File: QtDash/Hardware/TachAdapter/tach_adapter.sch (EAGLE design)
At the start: 10 parts, among them IC1 TLP293

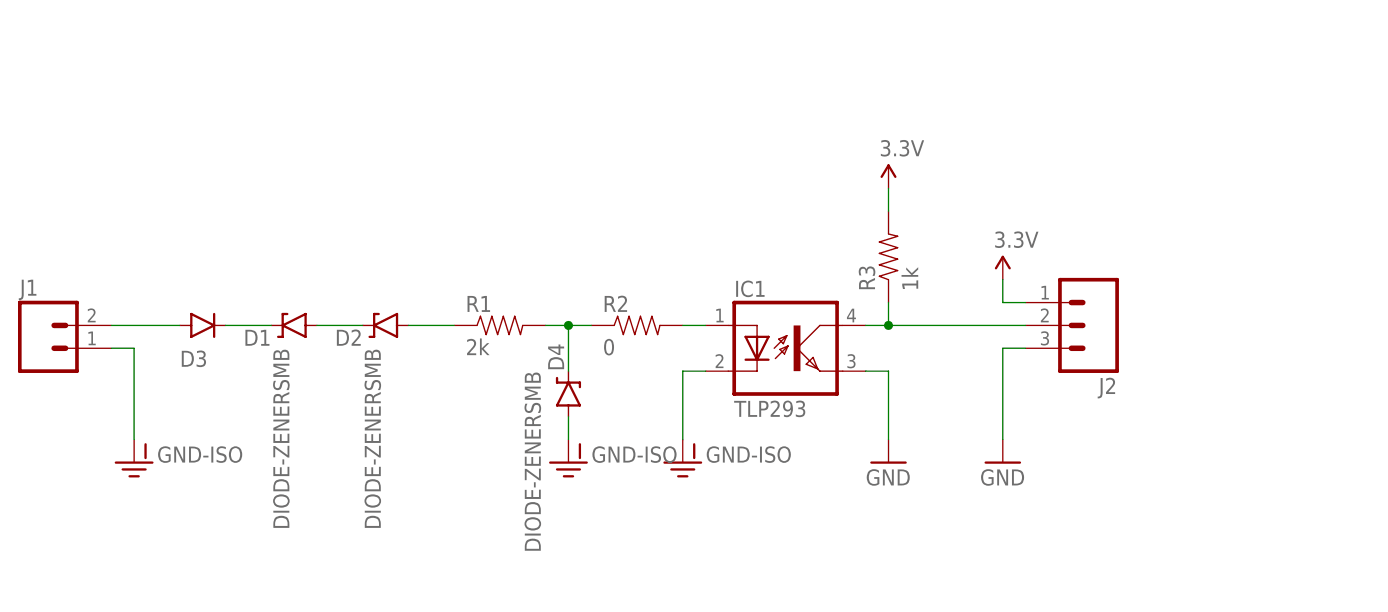
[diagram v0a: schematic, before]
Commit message: - updated tach adapter with opto-coupler that is currently available 	- added datasheets for tach-adapter components 	- updated dashhat library with new connector 31 dimensions 	- moved circuit simulations into their own folder
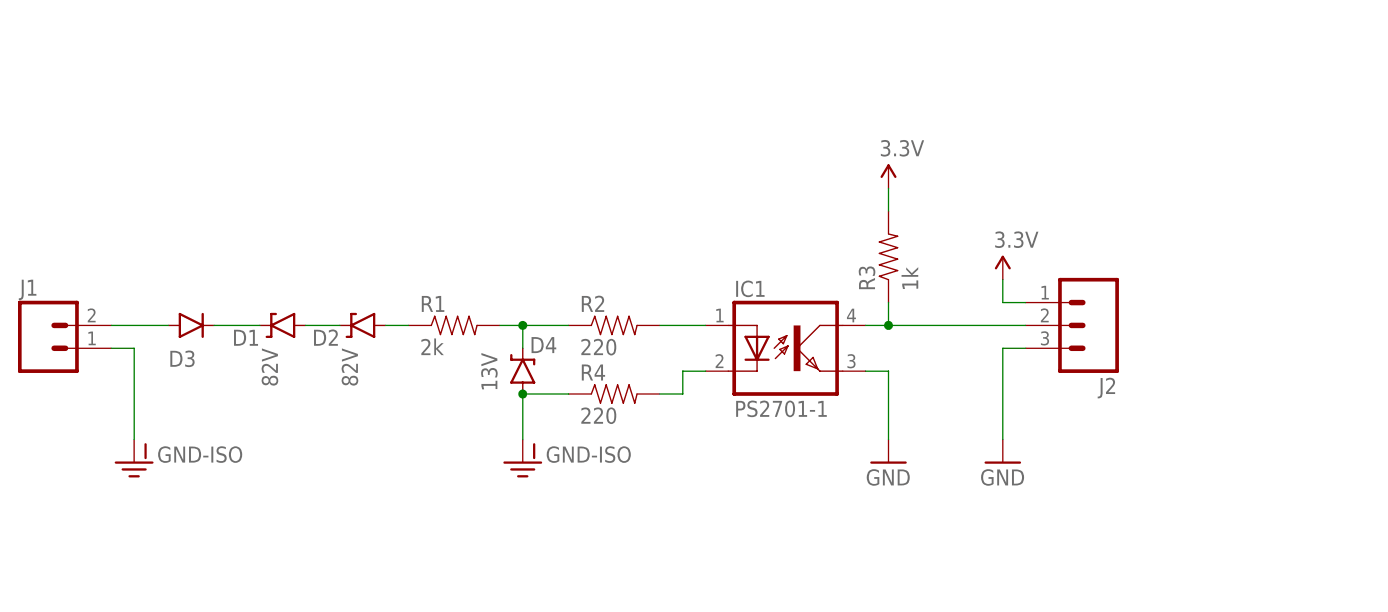
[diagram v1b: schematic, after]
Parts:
- added R4: 220, SparkFun-Passives:RESISTOR1206
- D1, D2: value DIODE-ZENERSMB -> 82V
- D4: value DIODE-ZENERSMB -> 13V
- IC1: value TLP293 -> PS2701-1; device tach_adapter:TLP293 -> tach_adapter:PS2701-1
- R2: value 0 -> 220
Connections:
- new net N$6: IC1.C, R4.2
- net GND-ISO: now also R4.1; no longer IC1.C
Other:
- moved on the sheet: D1, D2, D3, D4, R1, R2
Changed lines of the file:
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@@
 <?xml version="1.0" encoding="utf-8"?>
 <!DOCTYPE eagle SYSTEM "eagle.dtd">
-<eagle version="7.1.0">
+<eagle version="7.7.0">
 <drawing>
 <settings>
@@
 <setting verticaltext="up"/>
 </settings>
-<grid distance="0.1" unitdist="inch" unit="inch" style="lines" multiple="1" display="no" altdistance="0.01" altunitdist="inch" altunit="inch"/>
+<grid distance="0.05" unitdist="inch" unit="inch" style="lines" multiple="1" display="no" altdistance="0.01" altunitdist="inch" altunit="inch"/>
 <layers>
 <layer number="1" name="Top" color="4" fill="1" visible="no" active="no"/>
@@
 </classes>
 <parts>
-<part name="D1" library="SparkFun-DiscreteSemi" deviceset="DIODE-ZENER" device="SMB"/>
-<part name="D2" library="SparkFun-DiscreteSemi" deviceset="DIODE-ZENER" device="SMB"/>
+<part name="D1" library="SparkFun-DiscreteSemi" deviceset="DIODE-ZENER" device="SMB" value="82V"/>
+<part name="D2" library="SparkFun-DiscreteSemi" deviceset="DIODE-ZENER" device="SMB" value="82V"/>
 <part name="D3" library="SparkFun-DiscreteSemi" deviceset="DIODE" device="SMA"/>
 <part name="R1" library="SparkFun-Passives" deviceset="RESISTOR" device="1206" value="2k"/>
-<part name="R2" library="SparkFun-Passives" deviceset="RESISTOR" device="1206" value="0"/>
-<part name="IC1" library="tach_adapter" deviceset="TLP293" device=""/>
+<part name="R2" library="SparkFun-Passives" deviceset="RESISTOR" device="1206" value="220"/>
+<part name="IC1" library="tach_adapter" deviceset="PS2701-1" device=""/>
 <part name="R3" library="SparkFun-Passives" deviceset="RESISTOR" device="0603-RES" value="1k"/>
 <part name="SUPPLY1" library="SparkFun-Aesthetics" deviceset="3.3V" device=""/>
 <part name="GND1" library="SparkFun-Aesthetics" deviceset="GND" device=""/>
-<part name="GND-ISO1" library="SparkFun-Aesthetics" deviceset="GND-ISO" device=""/>
-<part name="D4" library="SparkFun-DiscreteSemi" deviceset="DIODE-ZENER" device="SMB"/>
+<part name="D4" library="SparkFun-DiscreteSemi" deviceset="DIODE-ZENER" device="SMB" value="13V"/>
 <part name="GND-ISO2" library="SparkFun-Aesthetics" deviceset="GND-ISO" device=""/>
 <part name="J1" library="SparkFun-Connectors" deviceset="M02" device="PTH3"/>
@@
 <part name="SUPPLY2" library="SparkFun-Aesthetics" deviceset="3.3V" device=""/>
 <part name="GND2" library="SparkFun-Aesthetics" deviceset="GND" device=""/>
+<part name="R4" library="SparkFun-Passives" deviceset="RESISTOR" device="1206" value="220"/>
 </parts>
 <sheets>
@@
 </plain>
 <instances>
-<instance part="D1" gate="G$1" x="45.72" y="60.96" smashed="yes" rot="R180">
-<attribute name="NAME" x="43.18" y="60.4774" size="1.778" layer="95" rot="R180"/>
-<attribute name="VALUE" x="43.4086" y="58.42" size="1.778" layer="96" rot="R270"/>
+<instance part="D1" gate="G$1" x="44.45" y="60.96" smashed="yes" rot="R180">
+<attribute name="NAME" x="41.91" y="60.4774" size="1.778" layer="95" rot="R180"/>
+<attribute name="VALUE" x="42.1386" y="58.42" size="1.778" layer="96" rot="R270"/>
 </instance>
-<instance part="D2" gate="G$1" x="55.88" y="60.96" smashed="yes" rot="R180">
-<attribute name="NAME" x="53.34" y="60.4774" size="1.778" layer="95" rot="R180"/>
-<attribute name="VALUE" x="53.5686" y="58.42" size="1.778" layer="96" rot="R270"/>
+<instance part="D2" gate="G$1" x="53.34" y="60.96" smashed="yes" rot="R180">
+<attribute name="NAME" x="50.8" y="60.4774" size="1.778" layer="95" rot="R180"/>
+<attribute name="VALUE" x="51.0286" y="58.42" size="1.778" layer="96" rot="R270"/>
 </instance>
-<instance part="D3" gate="G$1" x="35.56" y="60.96" smashed="yes">
-<attribute name="NAME" x="33.02" y="56.3626" size="1.778" layer="95"/>
-<attribute name="VALUE" x="38.1" y="58.6486" size="1.778" layer="96"/>
+<instance part="D3" gate="G$1" x="34.29" y="60.96" smashed="yes">
+<attribute name="NAME" x="31.75" y="56.3626" size="1.778" layer="95"/>
+<attribute name="VALUE" x="36.83" y="58.6486" size="1.778" layer="96"/>
 </instance>
-<instance part="R1" gate="G$1" x="68.58" y="60.96"/>
-<instance part="R2" gate="G$1" x="83.82" y="60.96"/>
+<instance part="R1" gate="G$1" x="63.5" y="60.96"/>
+<instance part="R2" gate="G$1" x="81.28" y="60.96"/>
 <instance part="IC1" gate="G$1" x="101.6" y="58.42"/>
 <instance part="R3" gate="G$1" x="111.76" y="68.58" rot="R90"/>
 <instance part="SUPPLY1" gate="G$1" x="111.76" y="76.2"/>
 <instance part="GND1" gate="1" x="111.76" y="45.72"/>
-<instance part="GND-ISO1" gate="G$1" x="88.9" y="45.72"/>
-<instance part="D4" gate="G$1" x="76.2" y="53.34" smashed="yes" rot="R90">
-<attribute name="NAME" x="75.7174" y="55.88" size="1.778" layer="95" rot="R90"/>
-<attribute name="VALUE" x="71.3486" y="55.88" size="1.778" layer="96" rot="R270"/>
+<instance part="D4" gate="G$1" x="71.12" y="55.88" smashed="yes" rot="R90">
+<attribute name="NAME" x="71.882" y="57.8866" size="1.778" layer="95"/>
+<attribute name="VALUE" x="66.5226" y="57.912" size="1.778" layer="96" rot="R270"/>
 </instance>
-<instance part="GND-ISO2" gate="G$1" x="76.2" y="45.72"/>
+<instance part="GND-ISO2" gate="G$1" x="71.12" y="45.72"/>
 <instance part="J1" gate="G$1" x="17.78" y="58.42"/>
 <instance part="J2" gate="J$1" x="134.62" y="60.96" rot="R180"/>
@@
 <instance part="SUPPLY2" gate="G$1" x="124.46" y="66.04"/>
 <instance part="GND2" gate="1" x="124.46" y="45.72"/>
+<instance part="R4" gate="G$1" x="81.28" y="53.34"/>
 </instances>
 <busses>
@@
 <pinref part="D1" gate="G$1" pin="C"/>
 <pinref part="D3" gate="G$1" pin="C"/>
-<wire x1="43.18" y1="60.96" x2="38.1" y2="60.96" width="0.1524" layer="91"/>
+<wire x1="41.91" y1="60.96" x2="36.83" y2="60.96" width="0.1524" layer="91"/>
 </segment>
 </net>
@@
 <pinref part="D1" gate="G$1" pin="A"/>
 <pinref part="D2" gate="G$1" pin="C"/>
-<wire x1="48.26" y1="60.96" x2="53.34" y2="60.96" width="0.1524" layer="91"/>
+<wire x1="46.99" y1="60.96" x2="50.8" y2="60.96" width="0.1524" layer="91"/>
 </segment>
 </net>
@@
 <pinref part="D2" gate="G$1" pin="A"/>
 <pinref part="R1" gate="G$1" pin="1"/>
-<wire x1="58.42" y1="60.96" x2="63.5" y2="60.96" width="0.1524" layer="91"/>
+<wire x1="55.88" y1="60.96" x2="58.42" y2="60.96" width="0.1524" layer="91"/>
 </segment>
 </net>
@@
 <pinref part="R1" gate="G$1" pin="2"/>
 <pinref part="R2" gate="G$1" pin="1"/>
-<wire x1="73.66" y1="60.96" x2="76.2" y2="60.96" width="0.1524" layer="91"/>
+<wire x1="68.58" y1="60.96" x2="71.12" y2="60.96" width="0.1524" layer="91"/>
 <pinref part="D4" gate="G$1" pin="C"/>
-<wire x1="76.2" y1="60.96" x2="78.74" y2="60.96" width="0.1524" layer="91"/>
-<wire x1="76.2" y1="55.88" x2="76.2" y2="60.96" width="0.1524" layer="91"/>
-<junction x="76.2" y="60.96"/>
+<wire x1="71.12" y1="60.96" x2="76.2" y2="60.96" width="0.1524" layer="91"/>
+<wire x1="71.12" y1="58.42" x2="71.12" y2="60.96" width="0.1524" layer="91"/>
+<junction x="71.12" y="60.96"/>
 </segment>
 </net>
@@
 <pinref part="R2" gate="G$1" pin="2"/>
 <pinref part="IC1" gate="G$1" pin="A"/>
-<wire x1="88.9" y1="60.96" x2="91.44" y2="60.96" width="0.1524" layer="91"/>
+<wire x1="86.36" y1="60.96" x2="91.44" y2="60.96" width="0.1524" layer="91"/>
 </segment>
 </net>
@@
 <net name="GND-ISO" class="0">
 <segment>
-<pinref part="IC1" gate="G$1" pin="C"/>
-<wire x1="91.44" y1="55.88" x2="88.9" y2="55.88" width="0.1524" layer="91"/>
-<pinref part="GND-ISO1" gate="G$1" pin="GND-ISO"/>
-<wire x1="88.9" y1="55.88" x2="88.9" y2="48.26" width="0.1524" layer="91"/>
-</segment>
-<segment>
 <pinref part="D4" gate="G$1" pin="A"/>
-<wire x1="76.2" y1="50.8" x2="76.2" y2="48.26" width="0.1524" layer="91"/>
 <pinref part="GND-ISO2" gate="G$1" pin="GND-ISO"/>
+<pinref part="R4" gate="G$1" pin="1"/>
+<wire x1="71.12" y1="53.34" x2="71.12" y2="48.26" width="0.1524" layer="91"/>
+<wire x1="76.2" y1="53.34" x2="71.12" y2="53.34" width="0.1524" layer="91"/>
+<junction x="71.12" y="53.34"/>
 </segment>
 <segment>
@@
 <pinref part="D3" gate="G$1" pin="A"/>
 <pinref part="J1" gate="G$1" pin="2"/>
-<wire x1="25.4" y1="60.96" x2="33.02" y2="60.96" width="0.1524" layer="91"/>
-</segment>
-</net>
+<wire x1="25.4" y1="60.96" x2="31.75" y2="60.96" width="0.1524" layer="91"/>
+</segment>
+</net>
+<net name="N$6" class="0">
+<segment>
+<pinref part="IC1" gate="G$1" pin="C"/>
+<wire x1="91.44" y1="55.88" x2="88.9" y2="55.88" width="0.1524" layer="91"/>
+<wire x1="88.9" y1="55.88" x2="88.9" y2="53.34" width="0.1524" layer="91"/>
+<pinref part="R4" gate="G$1" pin="2"/>
+<wire x1="88.9" y1="53.34" x2="86.36" y2="53.34" width="0.1524" layer="91"/>
+</segment>
+</net>

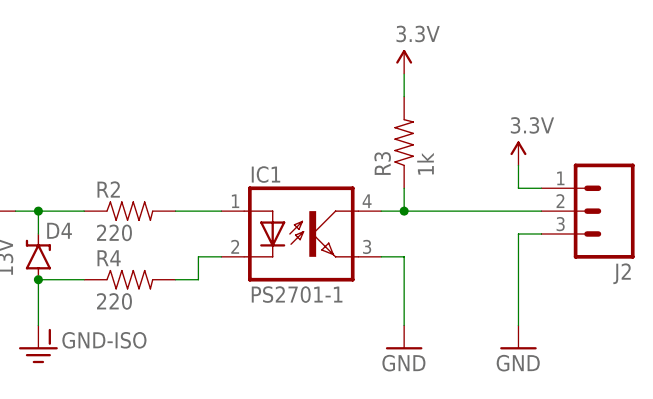
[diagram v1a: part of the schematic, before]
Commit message: - finished tach adapter board -- ordered components and board from OSHPark
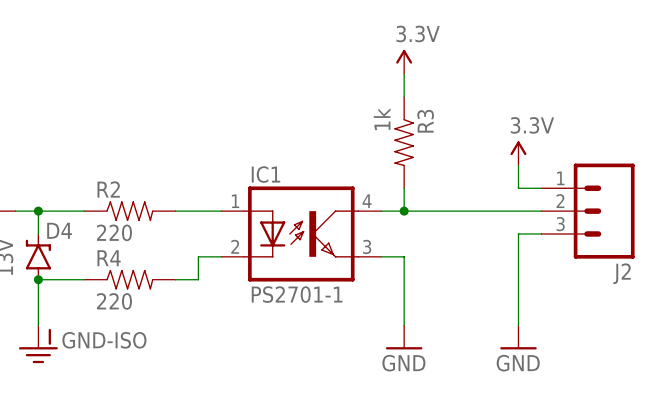
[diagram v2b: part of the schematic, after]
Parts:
- R3: device SparkFun-Passives:RESISTOR0603-RES -> SparkFun-Passives:RESISTOR1206
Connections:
- net 3.3V: now also R3.1; no longer R3.2
- net N$7: now also R3.2; no longer R3.1
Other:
- moved on the sheet: R3
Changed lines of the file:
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@@
 <setting verticaltext="up"/>
 </settings>
-<grid distance="0.05" unitdist="inch" unit="inch" style="lines" multiple="1" display="no" altdistance="0.01" altunitdist="inch" altunit="inch"/>
+<grid distance="0.1" unitdist="inch" unit="inch" style="lines" multiple="1" display="no" altdistance="0.01" altunitdist="inch" altunit="inch"/>
 <layers>
 <layer number="1" name="Top" color="4" fill="1" visible="no" active="no"/>
@@
 <part name="R2" library="SparkFun-Passives" deviceset="RESISTOR" device="1206" value="220"/>
 <part name="IC1" library="tach_adapter" deviceset="PS2701-1" device=""/>
-<part name="R3" library="SparkFun-Passives" deviceset="RESISTOR" device="0603-RES" value="1k"/>
 <part name="SUPPLY1" library="SparkFun-Aesthetics" deviceset="3.3V" device=""/>
 <part name="GND1" library="SparkFun-Aesthetics" deviceset="GND" device=""/>
@@
 <part name="GND2" library="SparkFun-Aesthetics" deviceset="GND" device=""/>
 <part name="R4" library="SparkFun-Passives" deviceset="RESISTOR" device="1206" value="220"/>
+<part name="R3" library="SparkFun-Passives" deviceset="RESISTOR" device="1206" value="1k"/>
 </parts>
 <sheets>
@@
 <instance part="R2" gate="G$1" x="81.28" y="60.96"/>
 <instance part="IC1" gate="G$1" x="101.6" y="58.42"/>
-<instance part="R3" gate="G$1" x="111.76" y="68.58" rot="R90"/>
 <instance part="SUPPLY1" gate="G$1" x="111.76" y="76.2"/>
 <instance part="GND1" gate="1" x="111.76" y="45.72"/>
@@
 <instance part="GND2" gate="1" x="124.46" y="45.72"/>
 <instance part="R4" gate="G$1" x="81.28" y="53.34"/>
+<instance part="R3" gate="G$1" x="111.76" y="68.58" rot="R270"/>
 </instances>
 <busses>
@@
 <wire x1="109.22" y1="60.96" x2="111.76" y2="60.96" width="0.1524" layer="91"/>
 <wire x1="111.76" y1="60.96" x2="111.76" y2="63.5" width="0.1524" layer="91"/>
-<pinref part="R3" gate="G$1" pin="1"/>
 <pinref part="J2" gate="J$1" pin="2"/>
 <wire x1="127" y1="60.96" x2="111.76" y2="60.96" width="0.1524" layer="91"/>
 <junction x="111.76" y="60.96"/>
+<pinref part="R3" gate="G$1" pin="2"/>
 </segment>
 </net>
 <net name="3.3V" class="0">
 <segment>
-<pinref part="R3" gate="G$1" pin="2"/>
 <pinref part="SUPPLY1" gate="G$1" pin="3.3V"/>
 <wire x1="111.76" y1="73.66" x2="111.76" y2="76.2" width="0.1524" layer="91"/>
-</segment>
-<segment>
+<pinref part="R3" gate="G$1" pin="1"/>
+</segment>
+<segment>

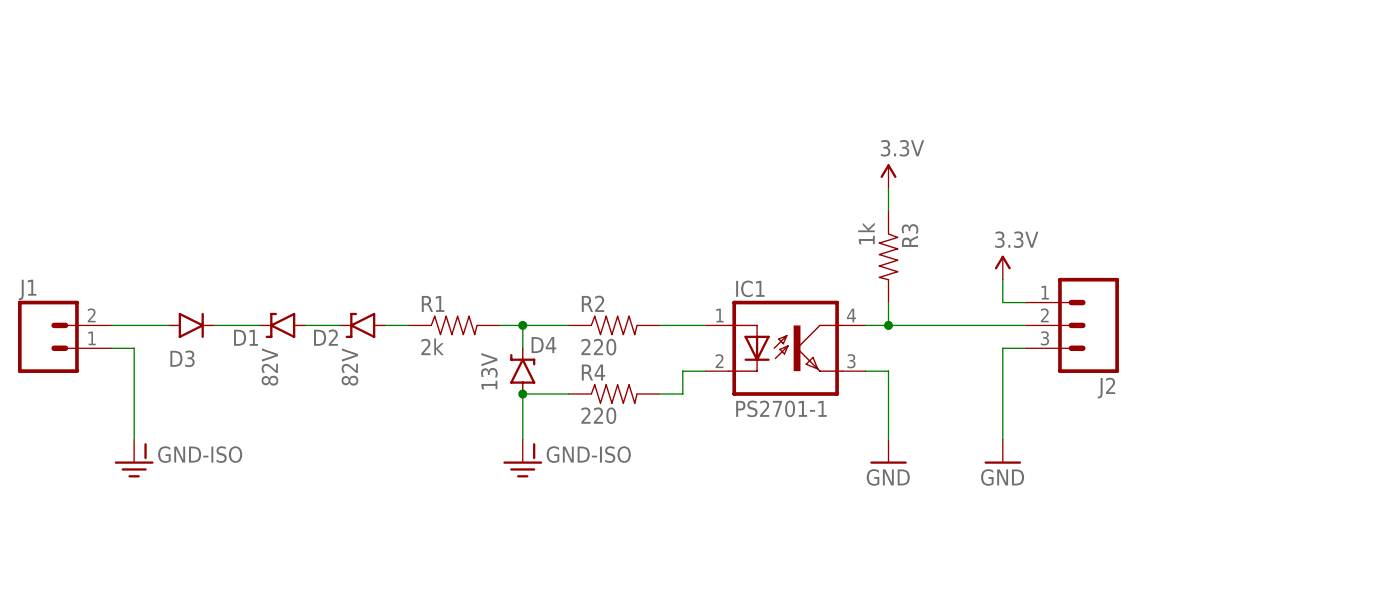
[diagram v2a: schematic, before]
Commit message: bugfix/hardware-revA-issues 	- removed superfluous zener diodes from input of tach adapter board 	- changed input/output wire solder hole sizes 	- added debouncing circuit that probably won't work on the output.
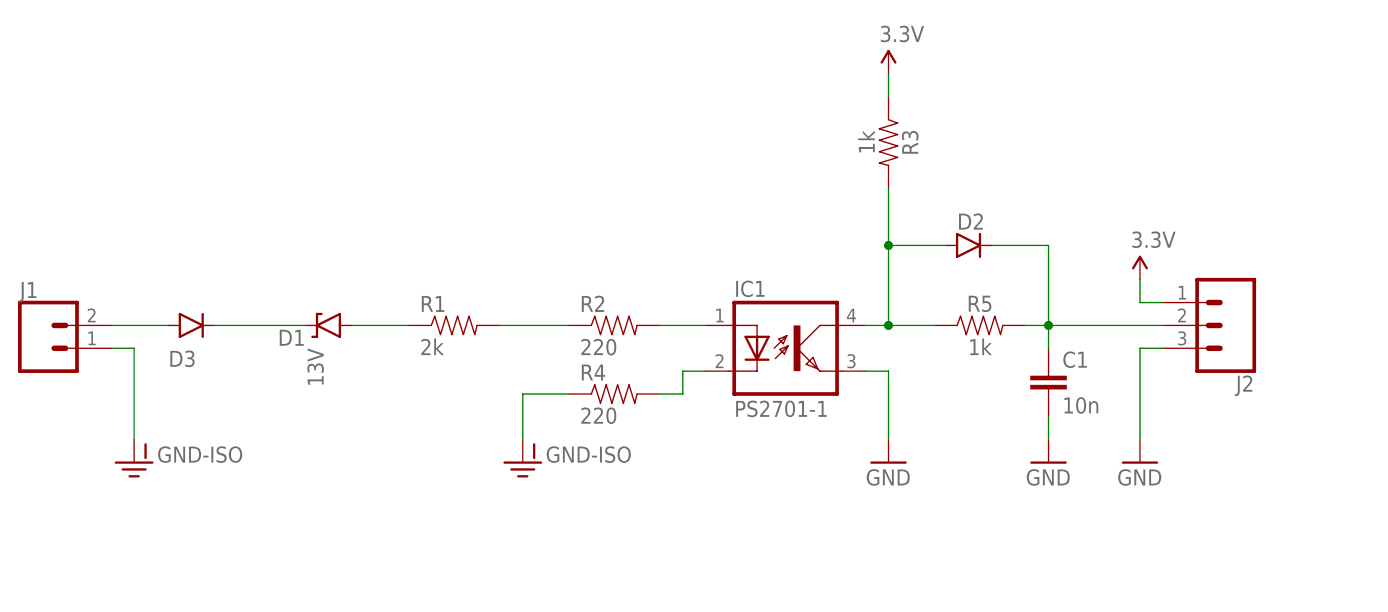
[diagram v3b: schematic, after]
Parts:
- removed D4: 13V, SparkFun-DiscreteSemi:DIODE-ZENERSMB
- added C1: 10n, digital_dash:CL10B103KB8NNNC
- added R5: 1k, digital_dash:RC0603JR-071KL
- D1: value 82V -> 13V
- D2: value 82V -> (none); device SparkFun-DiscreteSemi:DIODE-ZENERSMB -> SparkFun-DiscreteSemi:DIODESMA
- J1: device SparkFun-Connectors:M02PTH3 -> digital_dash:CONN_02LARGE
- J2: device SparkFun-Connectors:M03LONGPADS -> digital_dash:CONN_031X03_LARGE
- R3: device SparkFun-Passives:RESISTOR1206 -> digital_dash:RC0603JR-071KL
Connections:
- net GND: now also C1.2
- net GND-ISO: no longer D4.A
- net N$2: now also C1.1, J2.2, R5.2; no longer D1.A
- net N$3: now also D1.A; no longer D2.A
- net N$4: no longer D4.C
- net N$7: now also D2.A, R5.1; no longer J2.2
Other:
- moved on the sheet: D1, J2, R3

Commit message: bugfix/tach-adapter-updates: 	- updated eagle tach adapter project
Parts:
- added C2: 100n, digital_dash:CL10B104MB8NNNC
- IC1: value PS2701-1 -> H11L1SR2VM; device tach_adapter:PS2701-1 -> tach_adapter:H11L1SR2VM
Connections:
- net 3.3V: now also C2.1, IC1.VCC
- net GND: now also C2.2, IC1.GND; no longer IC1.EMIT
- net N$7: now also IC1.VOUT; no longer IC1.COL
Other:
- moved on the sheet: C1, D1, D2, J2, R1, R2, R3, R4, R5
